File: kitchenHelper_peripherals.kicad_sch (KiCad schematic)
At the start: 30 parts, among them J1 Temp 1, J3 Temp 2, J4 DISP_HDR, Q3 SS8050-G, Q4 SS8050-G, Q5 SS8050-G, SW2 BTN_LEFT, SW3 BTN_RIGHT, SW4 RotaryEncoder_Switch

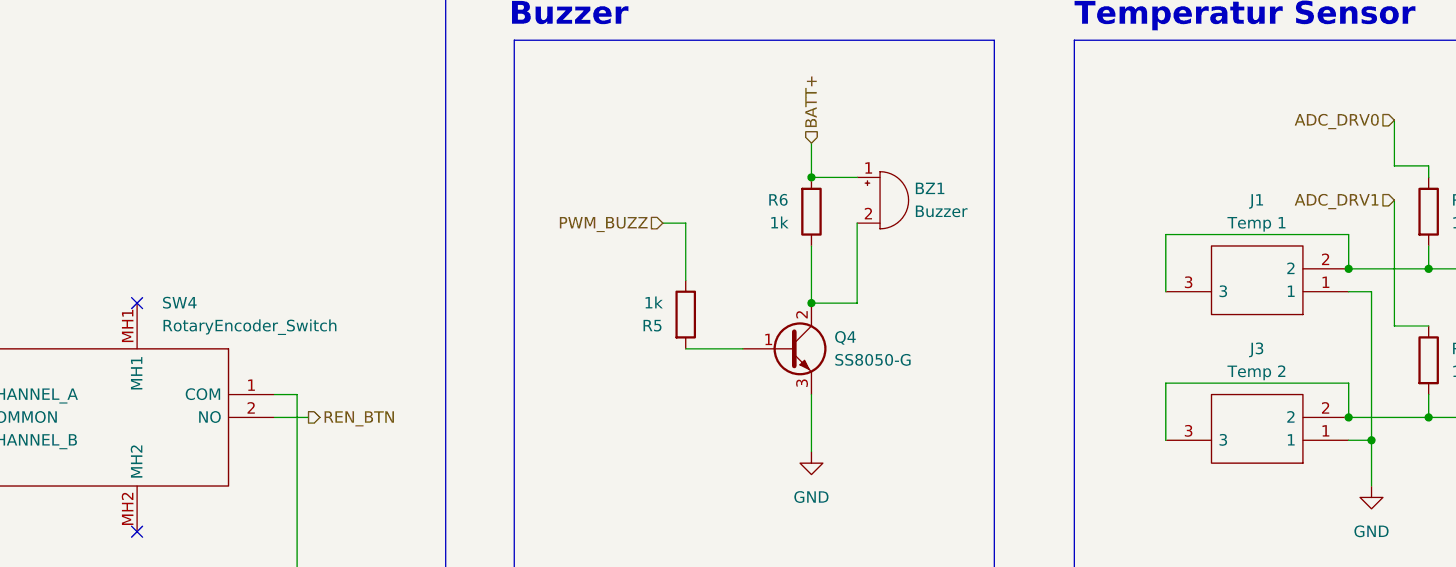
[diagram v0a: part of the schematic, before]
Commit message: Migrated project to KiCad7
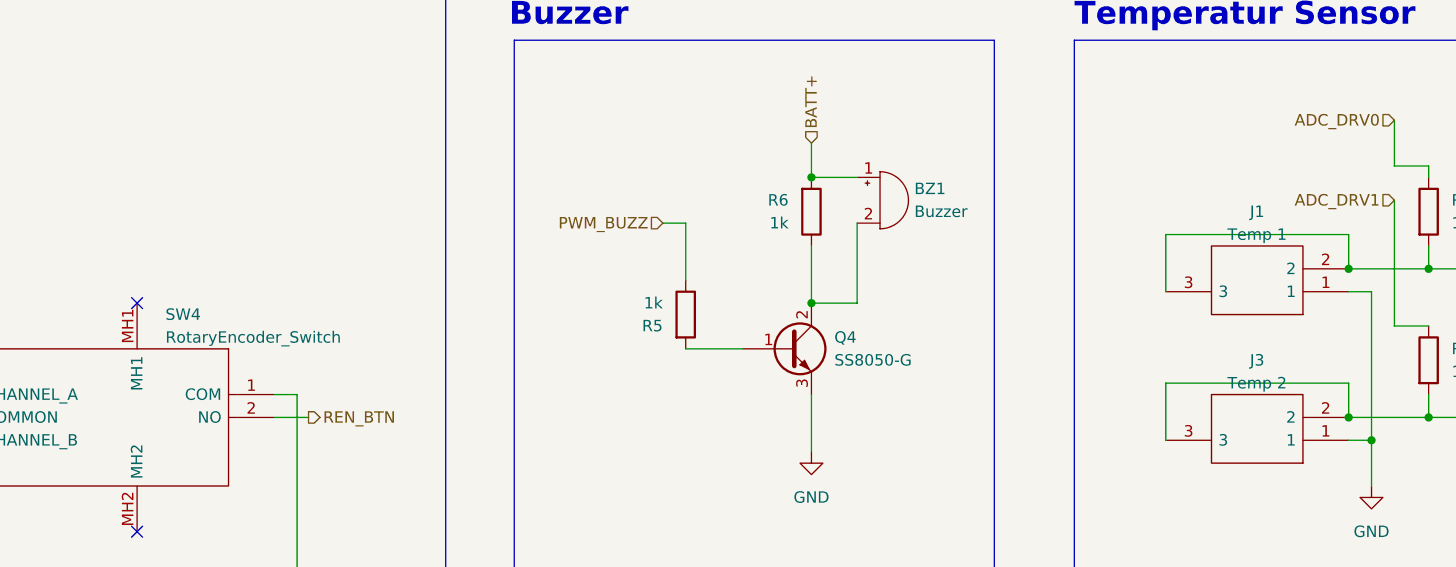
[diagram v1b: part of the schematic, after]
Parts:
- J1, J3: footprint footprints:MJ2509N -> MJ2509N; symbol MJ-2509N:MJ-2509N -> Connector_Audio:MJ-2509N
- SW4: footprint footprints:PEC12R3120FS0012 -> PEC12R3120FS0012; symbol PEC12R-3120F-S0012:PEC12R-3120F-S0012 -> Chof747 Controls:PEC12R-3120F-S0012
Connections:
- net +3V3: no longer J4.2 (Pin_2)
- new net +3.3V: J4.2 (Pin_2)
